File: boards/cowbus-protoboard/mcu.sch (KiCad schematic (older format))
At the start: 11 parts

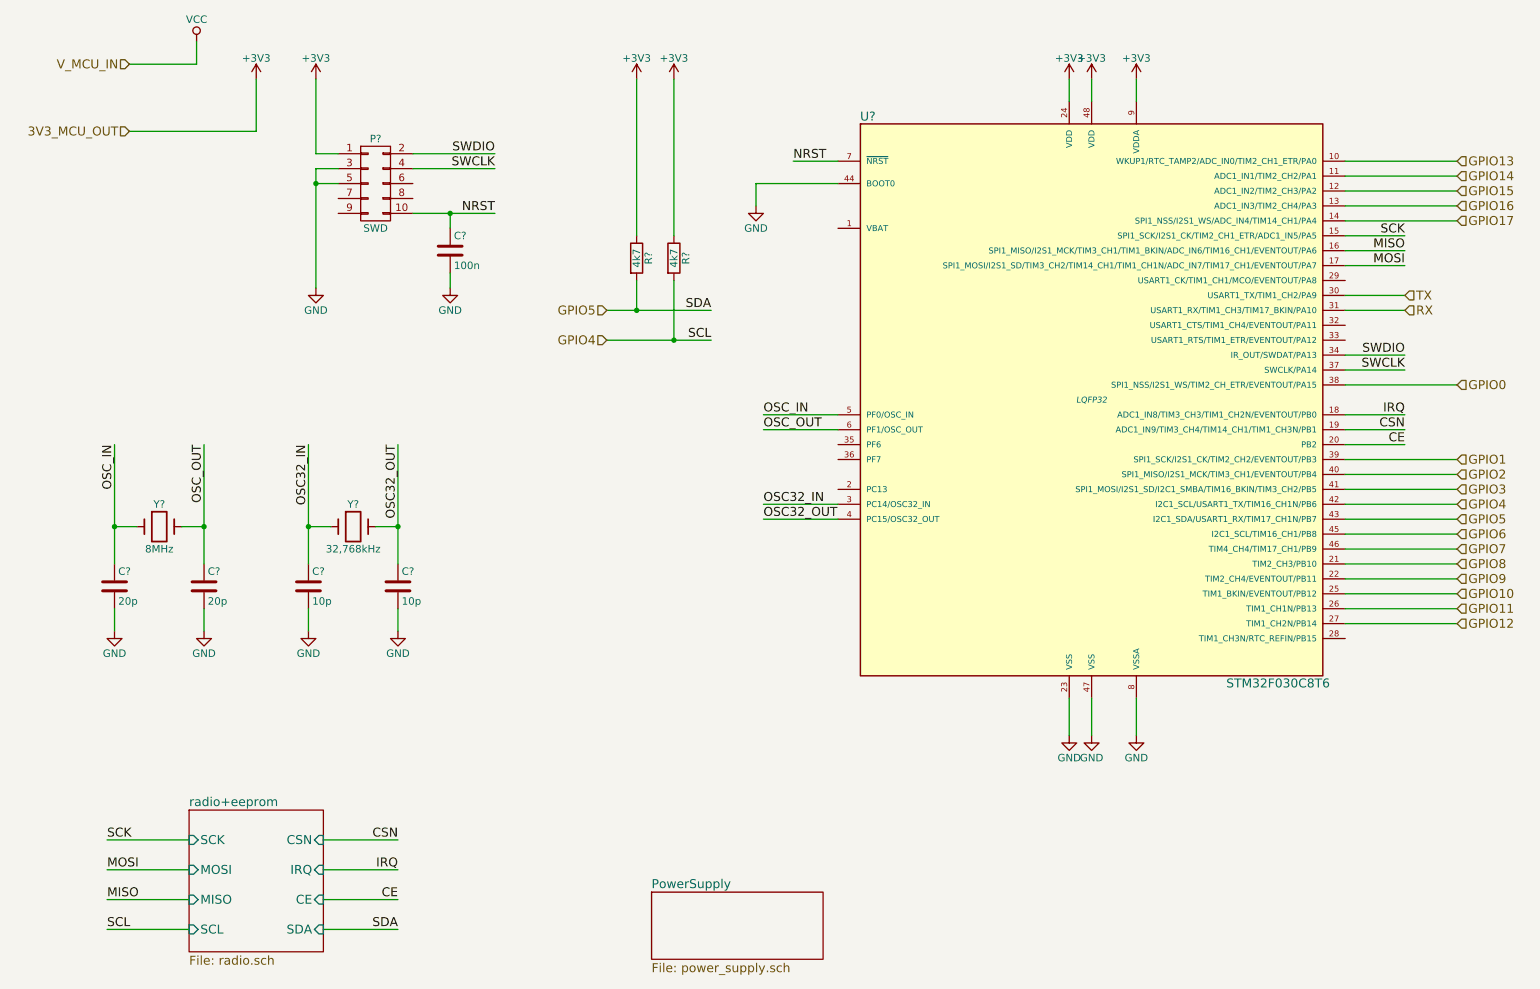
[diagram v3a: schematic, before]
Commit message: some footprint assignments done
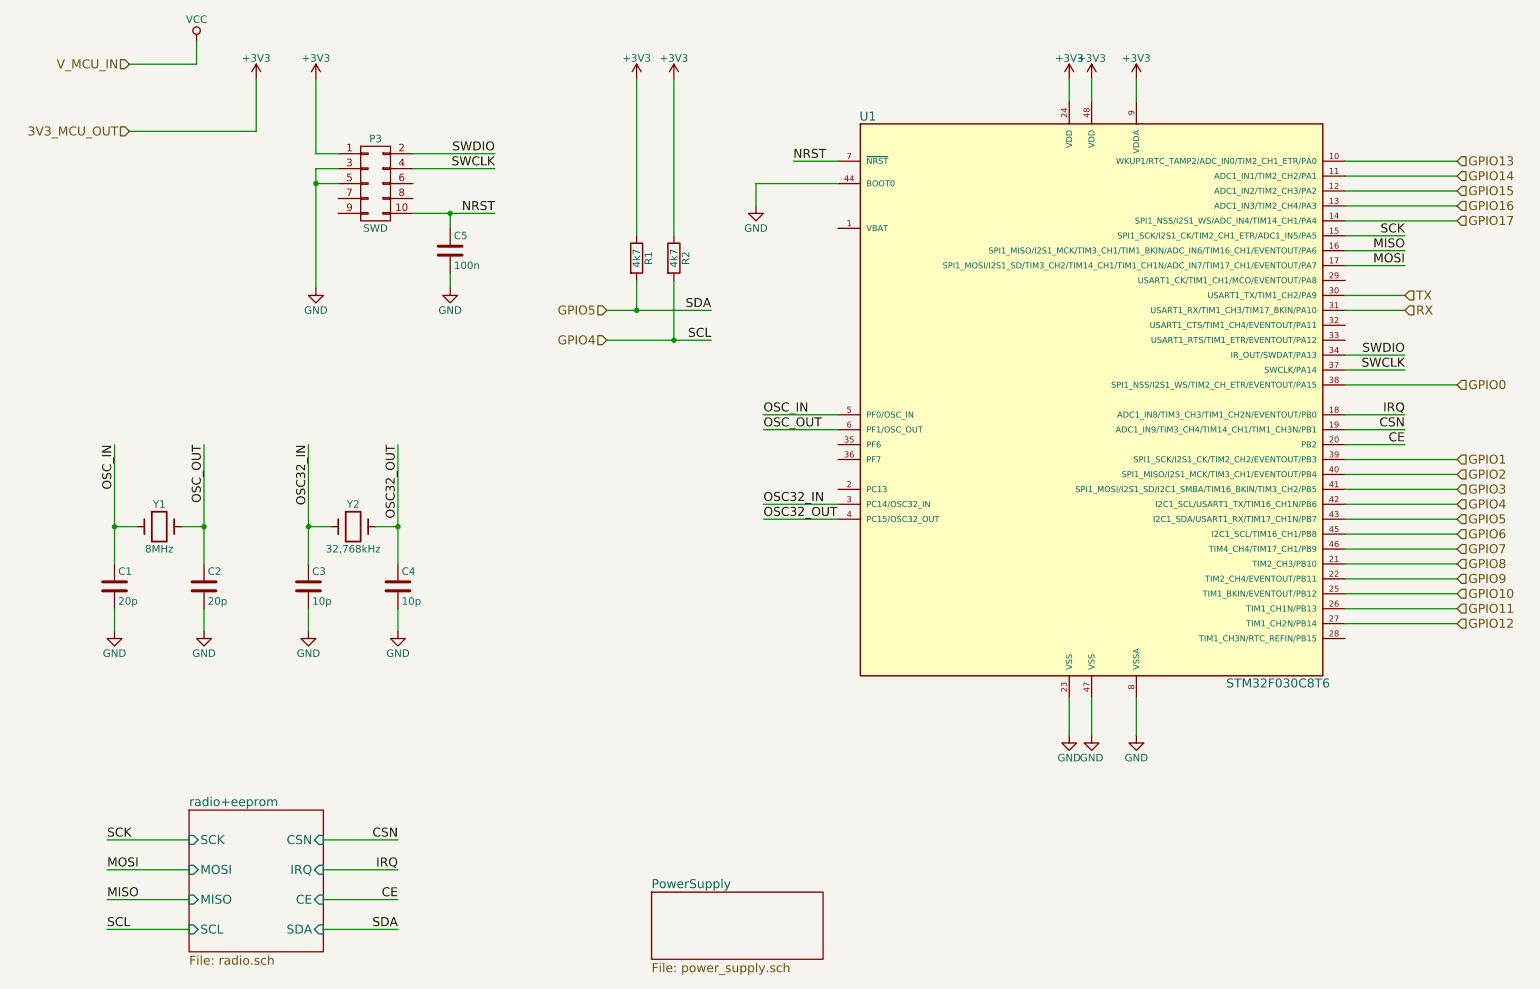
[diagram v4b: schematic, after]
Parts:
- C1, C2, C3, C4, C5: renamed from C?; footprint (none) -> Capacitors_SMD:C_0805_HandSoldering
- R1, R2: renamed from R?; footprint (none) -> Resistors_SMD:R_0805_HandSoldering
- U1: renamed from U?; footprint LQFP32 -> Housings_QFP:LQFP-48_7x7mm_Pitch0.5mm
- Y1: renamed from Y?; footprint (none) -> Crystals:Crystal_HC49-SD_SMD
- gave numbers to parts that had none: 2
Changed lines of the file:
@@
 $EndDescr
 $Comp
-L STM32F030C8T6 U?
+L STM32F030C8T6 U1
 U 1 1 55A4F1CE
 P 7750 3300
-F 0 "U?" H 6250 5200 60  0000 C CNN
+F 0 "U1" H 6250 5200 60  0000 C CNN
 F 1 "STM32F030C8T6" H 9000 1400 60  0000 C CNN
-F 2 "LQFP32" H 7750 3300 40  0000 C CIN
+F 2 "Housings_QFP:LQFP-48_7x7mm_Pitch0.5mm" H 7750 3300 40  0001 C CIN
 F 3 "" H 7750 3300 60  0000 C CNN
 	1    7750 3300
@@
 $EndSheet
 $Comp
-L GND #PWR?
+L GND #PWR04
 U 1 1 55A547FE
 P 7600 5550
-F 0 "#PWR?" H 7600 5300 50  0001 C CNN
+F 0 "#PWR04" H 7600 5300 50  0001 C CNN
 F 1 "GND" H 7600 5400 50  0000 C CNN
 F 2 "" H 7600 5550 60  0000 C CNN
@@
 $EndComp
 $Comp
-L GND #PWR?
+L GND #PWR05
 U 1 1 55A54837
 P 7750 5550
-F 0 "#PWR?" H 7750 5300 50  0001 C CNN
+F 0 "#PWR05" H 7750 5300 50  0001 C CNN
 F 1 "GND" H 7750 5400 50  0000 C CNN
 F 2 "" H 7750 5550 60  0000 C CNN
@@
 $EndComp
 $Comp
-L GND #PWR?
+L GND #PWR06
 U 1 1 55A54869
 P 8050 5550
-F 0 "#PWR?" H 8050 5300 50  0001 C CNN
+F 0 "#PWR06" H 8050 5300 50  0001 C CNN
 F 1 "GND" H 8050 5400 50  0000 C CNN
 F 2 "" H 8050 5550 60  0000 C CNN
@@
 $EndComp
 $Comp
-L +3V3 #PWR?
+L +3V3 #PWR07
 U 1 1 55A548DE
 P 7600 1150
-F 0 "#PWR?" H 7600 1000 50  0001 C CNN
+F 0 "#PWR07" H 7600 1000 50  0001 C CNN
 F 1 "+3V3" H 7600 1290 50  0000 C CNN
 F 2 "" H 7600 1150 60  0000 C CNN
@@
 $EndComp
 $Comp
-L +3V3 #PWR?
+L +3V3 #PWR08
 U 1 1 55A54917
 P 7750 1150
-F 0 "#PWR?" H 7750 1000 50  0001 C CNN
+F 0 "#PWR08" H 7750 1000 50  0001 C CNN
 F 1 "+3V3" H 7750 1290 50  0000 C CNN
 F 2 "" H 7750 1150 60  0000 C CNN
@@
 $EndComp
 $Comp
-L +3V3 #PWR?
+L +3V3 #PWR09
 U 1 1 55A54949
 P 8050 1150
-F 0 "#PWR?" H 8050 1000 50  0001 C CNN
+F 0 "#PWR09" H 8050 1000 50  0001 C CNN
 F 1 "+3V3" H 8050 1290 50  0000 C CNN
 F 2 "" H 8050 1150 60  0000 C CNN
@@
 $EndComp
 $Comp
-L CONN_02X05 P?
+L CONN_02X05 P3
 U 1 1 55A56EE6
 P 2950 1850
-F 0 "P?" H 2950 2150 50  0000 C CNN
+F 0 "P3" H 2950 2150 50  0000 C CNN
 F 1 "SWD" H 2950 1550 50  0000 C CNN
-F 2 "" H 2950 650 60  0000 C CNN
+F 2 "" H 2950 650 60  0001 C CNN
 F 3 "" H 2950 650 60  0000 C CNN
 	1    2950 1850
@@
 $EndComp
 $Comp
-L +3V3 #PWR?
+L +3V3 #PWR010
 U 1 1 55A57211
 P 2550 1150
-F 0 "#PWR?" H 2550 1000 50  0001 C CNN
+F 0 "#PWR010" H 2550 1000 50  0001 C CNN
 F 1 "+3V3" H 2550 1290 50  0000 C CNN
 F 2 "" H 2550 1150 60  0000 C CNN
@@
 $EndComp
 $Comp
-L GND #PWR?
+L GND #PWR011
 U 1 1 55A5724D
 P 2550 2550
-F 0 "#PWR?" H 2550 2300 50  0001 C CNN
+F 0 "#PWR011" H 2550 2300 50  0001 C CNN
 F 1 "GND" H 2550 2400 50  0000 C CNN
 F 2 "" H 2550 2550 60  0000 C CNN
@@
 NRST
 $Comp
-L C C?
+L C C1
 U 1 1 55A5BADD
 P 1200 4550
-F 0 "C?" H 1225 4650 50  0000 L CNN
+F 0 "C1" H 1225 4650 50  0000 L CNN
 F 1 "20p" H 1225 4450 50  0000 L CNN
-F 2 "" H 1238 4400 30  0000 C CNN
+F 2 "Capacitors_SMD:C_0805_HandSoldering" H 1238 4400 30  0001 C CNN
 F 3 "" H 1200 4550 60  0000 C CNN
 	1    1200 4550
@@
 $EndComp
 $Comp
-L C C?
+L C C2
 U 1 1 55A5BBCA
 P 1800 4550
-F 0 "C?" H 1825 4650 50  0000 L CNN
+F 0 "C2" H 1825 4650 50  0000 L CNN
 F 1 "20p" H 1825 4450 50  0000 L CNN
-F 2 "" H 1838 4400 30  0000 C CNN
+F 2 "Capacitors_SMD:C_0805_HandSoldering" H 1838 4400 30  0001 C CNN
 F 3 "" H 1800 4550 60  0000 C CNN
 	1    1800 4550
@@
 $EndComp
 $Comp
-L Crystal Y?
+L Crystal Y1
 U 1 1 55A5BCB3
 P 1500 4150
-F 0 "Y?" H 1500 4300 50  0000 C CNN
+F 0 "Y1" H 1500 4300 50  0000 C CNN
 F 1 "8MHz" H 1500 4000 50  0000 C CNN
-F 2 "" H 1500 4150 60  0000 C CNN
+F 2 "Crystals:Crystal_HC49-SD_SMD" H 1500 4150 60  0001 C CNN
 F 3 "" H 1500 4150 60  0000 C CNN
 	1    1500 4150
@@
 $EndComp
 $Comp
-L GND #PWR?
+L GND #PWR012
 U 1 1 55A5CA36
 P 1200 4850
-F 0 "#PWR?" H 1200 4600 50  0001 C CNN
+F 0 "#PWR012" H 1200 4600 50  0001 C CNN
 F 1 "GND" H 1200 4700 50  0000 C CNN
 F 2 "" H 1200 4850 60  0000 C CNN
@@
 $EndComp
 $Comp
-L GND #PWR?
+L GND #PWR013
 U 1 1 55A5CA84
 P 1800 4850
-F 0 "#PWR?" H 1800 4600 50  0001 C CNN
+F 0 "#PWR013" H 1800 4600 50  0001 C CNN
 F 1 "GND" H 1800 4700 50  0000 C CNN
 F 2 "" H 1800 4850 60  0000 C CNN
@@
 OSC_OUT
 $Comp
-L C C?
+L C C3
 U 1 1 55A5D614
 P 2500 4550
-F 0 "C?" H 2525 4650 50  0000 L CNN
+F 0 "C3" H 2525 4650 50  0000 L CNN
 F 1 "10p" H 2525 4450 50  0000 L CNN
-F 2 "" H 2538 4400 30  0000 C CNN
+F 2 "Capacitors_SMD:C_0805_HandSoldering" H 2538 4400 30  0001 C CNN
 F 3 "" H 2500 4550 60  0000 C CNN
 	1    2500 4550
@@
 $EndComp
 $Comp
-L C C?
+L C C4
 U 1 1 55A5D61A
 P 3100 4550
-F 0 "C?" H 3125 4650 50  0000 L CNN
+F 0 "C4" H 3125 4650 50  0000 L CNN
 F 1 "10p" H 3125 4450 50  0000 L CNN
-F 2 "" H 3138 4400 30  0000 C CNN
+F 2 "Capacitors_SMD:C_0805_HandSoldering" H 3138 4400 30  0001 C CNN
 F 3 "" H 3100 4550 60  0000 C CNN
 	1    3100 4550
@@
 $EndComp
 $Comp
-L Crystal Y?
+L Crystal Y2
 U 1 1 55A5D620
 P 2800 4150
-F 0 "Y?" H 2800 4300 50  0000 C CNN
+F 0 "Y2" H 2800 4300 50  0000 C CNN
 F 1 "32,768kHz" H 2800 4000 50  0000 C CNN
-F 2 "" H 2800 4150 60  0000 C CNN
+F 2 "" H 2800 4150 60  0001 C CNN
 F 3 "" H 2800 4150 60  0000 C CNN
 	1    2800 4150
@@
 $EndComp
 $Comp
-L GND #PWR?
+L GND #PWR014
 U 1 1 55A5D626
 P 2500 4850
-F 0 "#PWR?" H 2500 4600 50  0001 C CNN
+F 0 "#PWR014" H 2500 4600 50  0001 C CNN
 F 1 "GND" H 2500 4700 50  0000 C CNN
 F 2 "" H 2500 4850 60  0000 C CNN
@@
 $EndComp
 $Comp
-L GND #PWR?
+L GND #PWR015
 U 1 1 55A5D62C
 P 3100 4850
-F 0 "#PWR?" H 3100 4600 50  0001 C CNN
+F 0 "#PWR015" H 3100 4600 50  0001 C CNN
 F 1 "GND" H 3100 4700 50  0000 C CNN
 F 2 "" H 3100 4850 60  0000 C CNN
@@
 CE
 $Comp
-L GND #PWR?
+L GND #PWR016
 U 1 1 55A57289
 P 3450 2550
-F 0 "#PWR?" H 3450 2300 50  0001 C CNN
+F 0 "#PWR016" H 3450 2300 50  0001 C CNN
 F 1 "GND" H 3450 2400 50  0000 C CNN
 F 2 "" H 3450 2550 60  0000 C CNN
@@
 $EndComp
 $Comp
-L GND #PWR?
+L GND #PWR017
 U 1 1 55A6DF93
 P 5500 2000
-F 0 "#PWR?" H 5500 1750 50  0001 C CNN
+F 0 "#PWR017" H 5500 1750 50  0001 C CNN
 F 1 "GND" H 5500 1850 50  0000 C CNN
 F 2 "" H 5500 2000 60  0000 C CNN
@@
 $EndComp
 $Comp
-L C C?
+L C C5
 U 1 1 55A6E479
 P 3450 2300
-F 0 "C?" H 3475 2400 50  0000 L CNN
+F 0 "C5" H 3475 2400 50  0000 L CNN
 F 1 "100n" H 3475 2200 50  0000 L CNN
-F 2 "" H 3488 2150 30  0000 C CNN
+F 2 "Capacitors_SMD:C_0805_HandSoldering" H 3488 2150 30  0001 C CNN
 F 3 "" H 3450 2300 60  0000 C CNN
 	1    3450 2300
@@
 Connection ~ 3450 2050
 $Comp
-L VCC #PWR?
+L VCC #PWR018
 U 1 1 55A61A9B
 P 1750 900
-F 0 "#PWR?" H 1750 750 50  0001 C CNN
+F 0 "#PWR018" H 1750 750 50  0001 C CNN
 F 1 "VCC" H 1750 1050 50  0000 C CNN
 F 2 "" H 1750 900 60  0000 C CNN
@@
 $EndComp
 $Comp
-L +3V3 #PWR?
+L +3V3 #PWR019
 U 1 1 55A61AE5
 P 2150 1150
-F 0 "#PWR?" H 2150 1000 50  0001 C CNN
+F 0 "#PWR019" H 2150 1000 50  0001 C CNN
 F 1 "+3V3" H 2150 1290 50  0000 C CNN
 F 2 "" H 2150 1150 60  0000 C CNN
@@
 SCL
 $Comp
-L R R?
+L R R1
 U 1 1 55A8ED0D
 P 4700 2350
-F 0 "R?" V 4780 2350 50  0000 C CNN
+F 0 "R1" V 4780 2350 50  0000 C CNN
 F 1 "4k7" V 4700 2350 50  0000 C CNN
-F 2 "" V 4630 2350 30  0000 C CNN
+F 2 "Resistors_SMD:R_0805_HandSoldering" V 4630 2350 30  0001 C CNN
 F 3 "" H 4700 2350 30  0000 C CNN
 	1    4700 2350
@@
 $EndComp
 $Comp
-L R R?
+L R R2
 U 1 1 55A8EDC5
 P 4950 2350
-F 0 "R?" V 5030 2350 50  0000 C CNN
+F 0 "R2" V 5030 2350 50  0000 C CNN
 F 1 "4k7" V 4950 2350 50  0000 C CNN
-F 2 "" V 4880 2350 30  0000 C CNN
+F 2 "Resistors_SMD:R_0805_HandSoldering" V 4880 2350 30  0001 C CNN
 F 3 "" H 4950 2350 30  0000 C CNN
 	1    4950 2350
@@
 Connection ~ 4950 2900
 $Comp
-L +3V3 #PWR?
+L +3V3 #PWR020
 U 1 1 55A90A74
 P 4700 1150
-F 0 "#PWR?" H 4700 1000 50  0001 C CNN
+F 0 "#PWR020" H 4700 1000 50  0001 C CNN
 F 1 "+3V3" H 4700 1290 50  0000 C CNN
 F 2 "" H 4700 1150 60  0000 C CNN
@@
 $EndComp
 $Comp
-L +3V3 #PWR?
+L +3V3 #PWR021
 U 1 1 55A90A7A
 P 4950 1150
-F 0 "#PWR?" H 4950 1000 50  0001 C CNN
+F 0 "#PWR021" H 4950 1000 50  0001 C CNN
 F 1 "+3V3" H 4950 1290 50  0000 C CNN
 F 2 "" H 4950 1150 60  0000 C CNN

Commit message: first version of layout for protoboard
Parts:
- P3: footprint (none) -> lib:CORTEX_header_SMD
- Y2: footprint (none) -> lib:crystal_SMD_CPFB
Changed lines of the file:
@@
 EESchema Schematic File Version 2
+LIBS:cowbus-protoboard-rescue
 LIBS:power
 LIBS:device
@@
 LIBS:nrf24l01plus-module
 LIBS:i2c
+LIBS:led_rgb_reichelt
 LIBS:cowbus-protoboard-cache
 EELAYER 25 0
@@
 $EndSheet
 $Comp
-L GND #PWR04
+L GND #PWR18
 U 1 1 55A547FE
 P 7600 5550
-F 0 "#PWR04" H 7600 5300 50  0001 C CNN
+F 0 "#PWR18" H 7600 5300 50  0001 C CNN
 F 1 "GND" H 7600 5400 50  0000 C CNN
 F 2 "" H 7600 5550 60  0000 C CNN
@@
 $EndComp
 $Comp
-L GND #PWR05
+L GND #PWR20
 U 1 1 55A54837
 P 7750 5550
-F 0 "#PWR05" H 7750 5300 50  0001 C CNN
+F 0 "#PWR20" H 7750 5300 50  0001 C CNN
 F 1 "GND" H 7750 5400 50  0000 C CNN
 F 2 "" H 7750 5550 60  0000 C CNN
@@
 $EndComp
 $Comp
-L GND #PWR06
+L GND #PWR22
 U 1 1 55A54869
 P 8050 5550
-F 0 "#PWR06" H 8050 5300 50  0001 C CNN
+F 0 "#PWR22" H 8050 5300 50  0001 C CNN
 F 1 "GND" H 8050 5400 50  0000 C CNN
 F 2 "" H 8050 5550 60  0000 C CNN
@@
 $EndComp
 $Comp
-L +3V3 #PWR07
+L +3V3 #PWR17
 U 1 1 55A548DE
 P 7600 1150
-F 0 "#PWR07" H 7600 1000 50  0001 C CNN
+F 0 "#PWR17" H 7600 1000 50  0001 C CNN
 F 1 "+3V3" H 7600 1290 50  0000 C CNN
 F 2 "" H 7600 1150 60  0000 C CNN
@@
 $EndComp
 $Comp
-L +3V3 #PWR08
+L +3V3 #PWR19
 U 1 1 55A54917
 P 7750 1150
-F 0 "#PWR08" H 7750 1000 50  0001 C CNN
+F 0 "#PWR19" H 7750 1000 50  0001 C CNN
 F 1 "+3V3" H 7750 1290 50  0000 C CNN
 F 2 "" H 7750 1150 60  0000 C CNN
@@
 $EndComp
 $Comp
-L +3V3 #PWR09
+L +3V3 #PWR21
 U 1 1 55A54949
 P 8050 1150
-F 0 "#PWR09" H 8050 1000 50  0001 C CNN
+F 0 "#PWR21" H 8050 1000 50  0001 C CNN
 F 1 "+3V3" H 8050 1290 50  0000 C CNN
 F 2 "" H 8050 1150 60  0000 C CNN
@@
 F 0 "P3" H 2950 2150 50  0000 C CNN
 F 1 "SWD" H 2950 1550 50  0000 C CNN
-F 2 "" H 2950 650 60  0001 C CNN
+F 2 "lib:CORTEX_header_SMD" H 2950 650 60  0001 C CNN
 F 3 "" H 2950 650 60  0000 C CNN
 	1    2950 1850
@@
 $EndComp
 $Comp
-L +3V3 #PWR010
+L +3V3 #PWR10
 U 1 1 55A57211
 P 2550 1150
-F 0 "#PWR010" H 2550 1000 50  0001 C CNN
+F 0 "#PWR10" H 2550 1000 50  0001 C CNN
 F 1 "+3V3" H 2550 1290 50  0000 C CNN
 F 2 "" H 2550 1150 60  0000 C CNN
@@
 $EndComp
 $Comp
-L GND #PWR011
+L GND #PWR11
 U 1 1 55A5724D
 P 2550 2550
-F 0 "#PWR011" H 2550 2300 50  0001 C CNN
+F 0 "#PWR11" H 2550 2300 50  0001 C CNN
 F 1 "GND" H 2550 2400 50  0000 C CNN
 F 2 "" H 2550 2550 60  0000 C CNN
@@
 $EndComp
 $Comp
-L GND #PWR012
+L GND #PWR5
 U 1 1 55A5CA36
 P 1200 4850
-F 0 "#PWR012" H 1200 4600 50  0001 C CNN
+F 0 "#PWR5" H 1200 4600 50  0001 C CNN
 F 1 "GND" H 1200 4700 50  0000 C CNN
 F 2 "" H 1200 4850 60  0000 C CNN
@@
 $EndComp
 $Comp
-L GND #PWR013
+L GND #PWR7
 U 1 1 55A5CA84
 P 1800 4850
-F 0 "#PWR013" H 1800 4600 50  0001 C CNN
+F 0 "#PWR7" H 1800 4600 50  0001 C CNN
 F 1 "GND" H 1800 4700 50  0000 C CNN
 F 2 "" H 1800 4850 60  0000 C CNN
@@
 F 0 "Y2" H 2800 4300 50  0000 C CNN
 F 1 "32,768kHz" H 2800 4000 50  0000 C CNN
-F 2 "" H 2800 4150 60  0001 C CNN
+F 2 "lib:crystal_SMD_CPFB" H 2800 4150 60  0001 C CNN
 F 3 "" H 2800 4150 60  0000 C CNN
 	1    2800 4150
@@
 $EndComp
 $Comp
-L GND #PWR014
+L GND #PWR9
 U 1 1 55A5D626
 P 2500 4850
-F 0 "#PWR014" H 2500 4600 50  0001 C CNN
+F 0 "#PWR9" H 2500 4600 50  0001 C CNN
 F 1 "GND" H 2500 4700 50  0000 C CNN
 F 2 "" H 2500 4850 60  0000 C CNN
@@
 $EndComp
 $Comp
-L GND #PWR015
+L GND #PWR12
 U 1 1 55A5D62C
 P 3100 4850
-F 0 "#PWR015" H 3100 4600 50  0001 C CNN
+F 0 "#PWR12" H 3100 4600 50  0001 C CNN
 F 1 "GND" H 3100 4700 50  0000 C CNN
 F 2 "" H 3100 4850 60  0000 C CNN
@@
 CE
 $Comp
-L GND #PWR016
+L GND #PWR13
 U 1 1 55A57289
 P 3450 2550
-F 0 "#PWR016" H 3450 2300 50  0001 C CNN
+F 0 "#PWR13" H 3450 2300 50  0001 C CNN
 F 1 "GND" H 3450 2400 50  0000 C CNN
 F 2 "" H 3450 2550 60  0000 C CNN
@@
 $EndComp
 $Comp
-L GND #PWR017
+L GND #PWR16
 U 1 1 55A6DF93
 P 5500 2000
-F 0 "#PWR017" H 5500 1750 50  0001 C CNN
+F 0 "#PWR16" H 5500 1750 50  0001 C CNN
 F 1 "GND" H 5500 1850 50  0000 C CNN
 F 2 "" H 5500 2000 60  0000 C CNN
@@
 Connection ~ 3450 2050
 $Comp
-L VCC #PWR018
+L VCC #PWR6
 U 1 1 55A61A9B
 P 1750 900
-F 0 "#PWR018" H 1750 750 50  0001 C CNN
+F 0 "#PWR6" H 1750 750 50  0001 C CNN
 F 1 "VCC" H 1750 1050 50  0000 C CNN
 F 2 "" H 1750 900 60  0000 C CNN
@@
 $EndComp
 $Comp
-L +3V3 #PWR019
+L +3V3 #PWR8
 U 1 1 55A61AE5
 P 2150 1150
-F 0 "#PWR019" H 2150 1000 50  0001 C CNN
+F 0 "#PWR8" H 2150 1000 50  0001 C CNN
 F 1 "+3V3" H 2150 1290 50  0000 C CNN
 F 2 "" H 2150 1150 60  0000 C CNN
@@
 Connection ~ 4950 2900
 $Comp
-L +3V3 #PWR020
+L +3V3 #PWR14
 U 1 1 55A90A74
 P 4700 1150
-F 0 "#PWR020" H 4700 1000 50  0001 C CNN
+F 0 "#PWR14" H 4700 1000 50  0001 C CNN
 F 1 "+3V3" H 4700 1290 50  0000 C CNN
 F 2 "" H 4700 1150 60  0000 C CNN
@@
 $EndComp
 $Comp
-L +3V3 #PWR021
+L +3V3 #PWR15
 U 1 1 55A90A7A
 P 4950 1150
-F 0 "#PWR021" H 4950 1000 50  0001 C CNN
+F 0 "#PWR15" H 4950 1000 50  0001 C CNN
 F 1 "+3V3" H 4950 1290 50  0000 C CNN
 F 2 "" H 4950 1150 60  0000 C CNN
